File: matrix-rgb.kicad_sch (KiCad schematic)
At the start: 29 parts

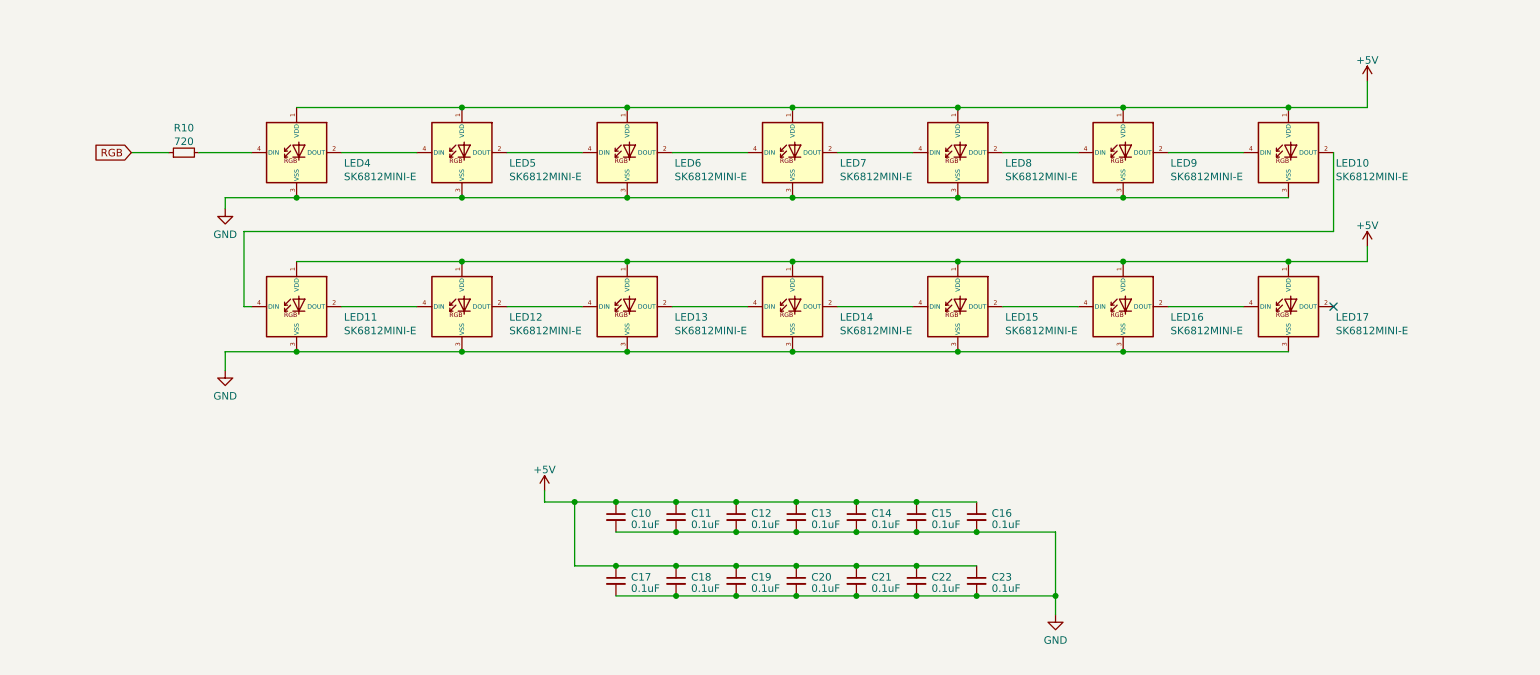
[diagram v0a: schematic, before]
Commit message: Rev 0.3
Might send this one out to get made. Not sure yet.

- Added 2 more LEDs to the edge and positioned them to be a little more evenly spread out.
- Rerouted all LED traces for better aesthetics and functionality.
- Increased power trace size. This might not be needed but it can't hurt to add with the addition of the LEDs.
- Removed programming headers. This was a personal decision as I never used them or found a need for them. It helped free up some space to route LEDs.
- Updated library, images, gerbies and BOM.
- Added a firmware that has not been tested yet, but should work in theory.
- No more position files. Too many issues at various fab houses with positions/parts/QA with previous boards.
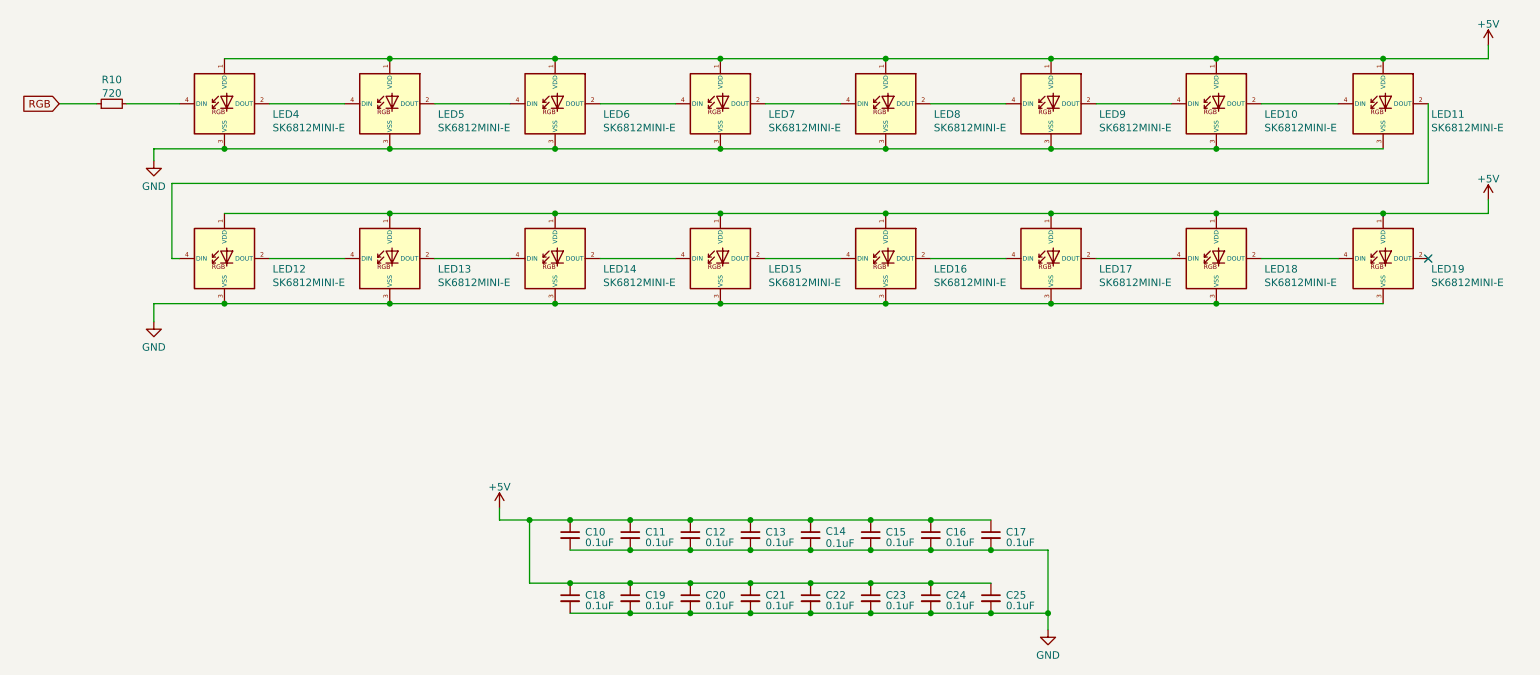
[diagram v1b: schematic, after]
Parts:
- removed LED12, LED15, LED8: SK6812MINI-E, arisutea:LED_SK6812MINI-E, symbol arisutea-pcb:LED_SK6812MINI-E
- added C24, C25: 0.1uF, arisutea:C_0805_2012Metric_Pad1.18x1.45mm_HandSolder, symbol arisutea-pcb:Device_C_Small
- added LED10, LED11, LED17, LED18, LED19: SK6812MINI-E, arisutea:LED_SK6812MINI-E, symbol arisutea-pcb:LED_SK6812MINI-E
- C10, C11, C12, C13, C14, C15, C16, C17, C18, C19, C20, C21, C22, C23: LCSC (none) -> C28233
- R10: LCSC (none) -> C17818
- renumbered LED11 to LED12, LED16 to LED15, LED17 to LED16, LED9 to LED8, LED10 to LED9
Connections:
- net +5V: now also C24.1, C25.1, LED10.1 (VDD), LED11.1 (VDD), LED17.1 (VDD), LED18.1 (VDD), LED19.1 (VDD)
- net GND: now also C24.2, C25.2, LED10.3 (VSS), LED11.3 (VSS), LED17.3 (VSS), LED18.3 (VSS), LED19.3 (VSS)
- net at LED13.4 (DIN): now also LED12.2 (DOUT)
- net at LED14.2 (DOUT): now also LED15.4 (DIN)
- net at LED16.2 (DOUT): now also LED17.4 (DIN)
- net at LED9.2 (DOUT): now also LED10.4 (DIN); no longer LED12.4 (DIN)
- net at LED8.4 (DIN): now also LED7.2 (DOUT)
- new net: LED10.2 (DOUT), LED11.4 (DIN)
- new net: LED17.2 (DOUT), LED18.4 (DIN)
- new net: LED11.2 (DOUT), LED12.4 (DIN)
- new net: LED18.2 (DOUT), LED19.4 (DIN)
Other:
- moved on the sheet: C10, C11, C12, C13, C14, C15, C16, C17, C18, C19, C20, C21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

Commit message: added MOAR LEDZZZZZZZZZ
5 more to be exact.
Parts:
- added C26, C27, C28, C29, C30: 0.1uF, arisutea:C_0805_2012Metric_Pad1.18x1.45mm_HandSolder, symbol arisutea-pcb:Device_C_Small
- added LED20, LED21, LED22, LED23, LED24: SK6812MINI-E, arisutea:LED_SK6812MINI-E, symbol arisutea-pcb:LED_SK6812MINI-E
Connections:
- net +5V: now also C26.1, C27.1, C28.1, C29.1, C30.1, LED20.1 (VDD), LED21.1 (VDD), LED22.1 (VDD), LED23.1 (VDD), LED24.1 (VDD)
- net GND: now also C26.2, C27.2, C28.2, C29.2, C30.2, LED20.3 (VSS), LED21.3 (VSS), LED22.3 (VSS), LED23.3 (VSS), LED24.3 (VSS)
- net at LED19.2 (DOUT): now also LED20.4 (DIN)
- new net: LED22.2 (DOUT), LED23.4 (DIN)
- new net: LED21.2 (DOUT), LED22.4 (DIN)
- new net: LED23.2 (DOUT), LED24.4 (DIN)
- new net: LED20.2 (DOUT), LED21.4 (DIN)
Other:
- moved on the sheet: C10, C11, C12, C13, C14, C15, C16, C17, C18, C19, C20, C21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
